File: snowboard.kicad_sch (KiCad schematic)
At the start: 62 parts, among them J1 Micro USB Port, J2 B2B-PH-K-S, Q1 S8050, Q2 S8050, SW1 BOOT, SW2 RESET, U1 ESP32-WROVER-E-N4R8, U2 CP2102N-A02-GQFN28R, U3 SPX3819M5-L-3-3, U4 MCP73831T-2ACI_OT, U5 MPU-6050

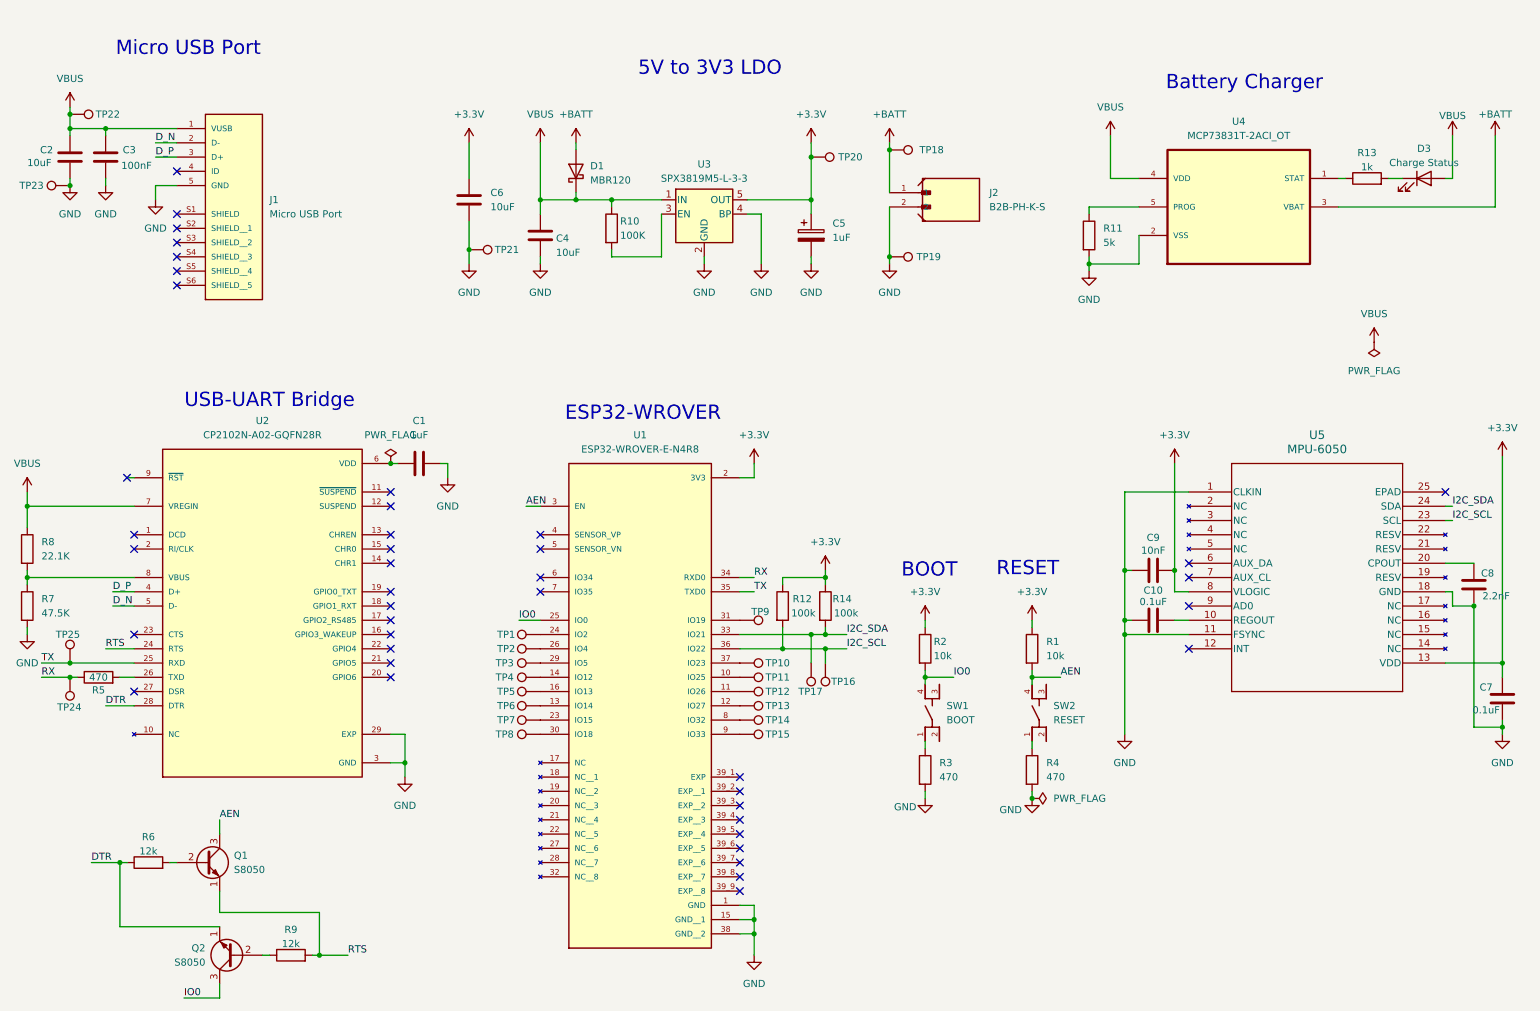
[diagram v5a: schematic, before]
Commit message: Swap discontinued MPU6050 for BNO086
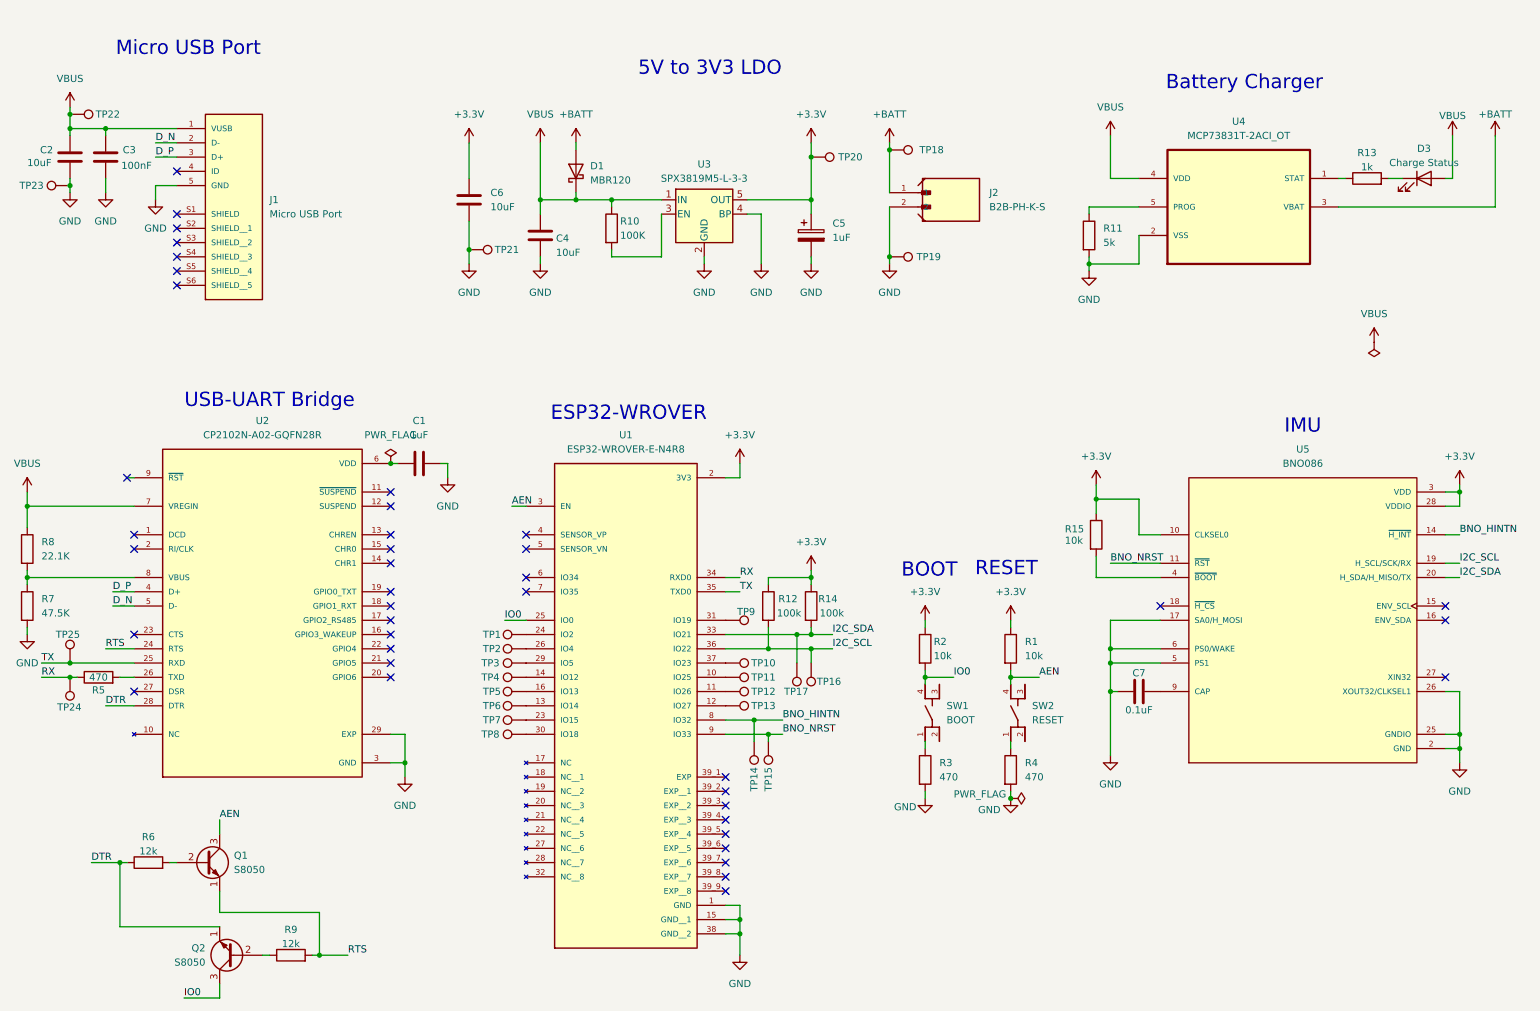
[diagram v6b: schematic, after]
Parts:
- removed C10: 0.1uF, symbol Device:C
- removed C8: 2.2nF, symbol Device:C
- removed C9: 10nF, symbol Device:C
- removed U5: MPU-6050, QFN24_4X4X0P9-0P5_TDK, symbol MPU6050:MPU-6050
- added R15: 10k, symbol Device:R
- added U5: BNO086, BNO080:IC_BNO080, symbol BNO086:BNO080
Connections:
- net +3.3V: now also R15.1, U5.10 (CLKSEL0), U5.28 (VDDIO), U5.3 (VDD); no longer C7.1
- net GND: now also C7.1, U5.17 (SA0/H_MOSI), U5.2 (GND), U5.25 (GNDIO), U5.26 (XOUT32/CLKSEL1), U5.5 (PS1), U5.6 (PS0/WAKE); no longer C7.2
- net I2C_SCL: now also U5.19 (H_SCL/SCK/RX)
- net I2C_SDA: now also U5.20 (H_SDA/H_MISO/TX)
- net BNO_NRST: now reaches TP15.1, U1.9 (IO33)
- net BNO_NRST: now also U5.11 (~{RST})
- net BNO_HINTN: now reaches TP14.1, U1.8 (IO32)
- net BNO_HINTN: now also U5.14 (~{H_INT})
- new net: R15.2, U5.4 (~{BOOT})
- new net: C7.2, U5.9 (CAP)
- no-connect marks 42 -> 41
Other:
- note added: "IMU"
- moved on the sheet: R1, R12, R14, R4, SW2, TP1, TP10, TP11, TP12, TP13, TP14, TP15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

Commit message: Reduce i2c pull-up value, fix shorting LDO, DNP auto-reset
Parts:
- Q1, Q2: now not fitted
- R12, R14: value 100k -> 5k
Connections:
- net GND: no longer U3.4 (BP)
- no-connect marks 41 -> 42
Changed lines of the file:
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@@
 (kicad_sch
-	(version 20231120)
+	(version 20250114)
 	(generator "eeschema")
-	(generator_version "8.0")
+	(generator_version "9.0")
 	(paper "A4")
+	(text "USB-UART Bridge\n"
+		(exclude_from_sim no)
+		(at 62.23 89.154 0)
+		(effects
+			(font
+				(size 2.54 2.54)
+			)
+		)
+	)
+	(text "IMU\n"
+		(exclude_from_sim no)
+		(at 246.38 93.726 0)
+		(effects
+			(font
+				(size 2.54 2.54)
+			)
+		)
+	)
+	(text "Battery Charger\n"
+		(exclude_from_sim no)
+		(at 235.966 32.512 0)
+		(effects
+			(font
+				(size 2.54 2.54)
+			)
+		)
+	)
+	(text "Micro USB Port\n"
+		(exclude_from_sim no)
+		(at 47.752 26.416 0)
+		(effects
+			(font
+				(size 2.54 2.54)
+			)
+		)
+	)
+	(text "ESP32-WROVER\n"
+		(exclude_from_sim no)
+		(at 126.238 91.44 0)
+		(effects
+			(font
+				(size 2.54 2.54)
+			)
+		)
+	)
+	(text "RESET\n"
+		(exclude_from_sim no)
+		(at 193.548 119.126 0)
+		(effects
+			(font
+				(size 2.54 2.54)
+			)
+		)
+	)
+	(text "5V to 3V3 LDO\n\n"
+		(exclude_from_sim no)
+		(at 140.716 32.004 0)
+		(effects
+			(font
+				(size 2.54 2.54)
+			)
+		)
+	)
+	(text "BOOT"
+		(exclude_from_sim no)
+		(at 179.832 119.38 0)
+		(effects
+			(font
+				(size 2.54 2.54)
+			)
+		)
+	)
 	(junction
 		(at 26.67 38.1)
@@
 	)
 	(no_connect
+		(at 147.32 55.88)
+	)
+	(no_connect
 		(at 107.95 120.65)
 	)
@@
 	(wire
 		(pts
-			(xy 149.86 55.88) (xy 149.86 64.77)
-		)
-		(stroke
-			(width 0)
-			(type default)
-		)
-	)
-	(wire
-		(pts
 			(xy 26.67 38.1) (xy 26.67 36.83)
 		)
@@
 	(wire
 		(pts
-			(xy 147.32 55.88) (xy 149.86 55.88)
-		)
-		(stroke
-			(width 0)
-			(type default)
-		)
-	)
-	(wire
-		(pts
 			(xy 110.49 43.18) (xy 110.49 53.34)
 		)
@@
 		)
 	)
-	(text "USB-UART Bridge\n"
-		(exclude_from_sim no)
-		(at 62.23 89.154 0)
-		(effects
-			(font
-				(size 2.54 2.54)
-			)
-		)
-	)
-	(text "IMU\n"
-		(exclude_from_sim no)
-		(at 246.38 93.726 0)
-		(effects
-			(font
-				(size 2.54 2.54)
-			)
-		)
-	)
-	(text "Battery Charger\n"
-		(exclude_from_sim no)
-		(at 235.966 32.512 0)
-		(effects
-			(font
-				(size 2.54 2.54)
-			)
-		)
-	)
-	(text "Micro USB Port\n"
-		(exclude_from_sim no)
-		(at 47.752 26.416 0)
-		(effects
-			(font
-				(size 2.54 2.54)
-			)
-		)
-	)
-	(text "ESP32-WROVER\n"
-		(exclude_from_sim no)
-		(at 126.238 91.44 0)
-		(effects
-			(font
-				(size 2.54 2.54)
-			)
-		)
-	)
-	(text "RESET\n"
-		(exclude_from_sim no)
-		(at 193.548 119.126 0)
-		(effects
-			(font
-				(size 2.54 2.54)
-			)
-		)
-	)
-	(text "5V to 3V3 LDO\n\n"
-		(exclude_from_sim no)
-		(at 140.716 32.004 0)
-		(effects
-			(font
-				(size 2.54 2.54)
-			)
-		)
-	)
-	(text "BOOT"
-		(exclude_from_sim no)
-		(at 179.832 119.38 0)
-		(effects
-			(font
-				(size 2.54 2.54)
-			)
-		)
-	)
 	(label "IO0"
 		(at 46.99 195.58 0)
@@
 			)
 		)
-		(property "Value" "100k"
+		(property "Value" "5k"
 			(at 152.654 127 0)
 			(effects
@@
 		(in_bom yes)
 		(on_board yes)
-		(dnp no)
+		(dnp yes)
 		(fields_autoplaced yes)
 		(property "Reference" "Q2"
@@
 		(in_bom yes)
 		(on_board yes)
-		(dnp no)
+		(dnp yes)
 		(fields_autoplaced yes)
 		(property "Reference" "Q1"
@@
 			)
 		)
-		(property "Value" "100k"
+		(property "Value" "5k"
 			(at 160.274 127 0)
 			(effects
@@
 	)
 	(symbol
-		(lib_id "power:GND")
-		(at 149.86 64.77 0)
-		(unit 1)
-		(exclude_from_sim no)
-		(in_bom yes)
-		(on_board yes)
-		(dnp no)
-		(fields_autoplaced yes)
-		(property "Reference" "#PWR020"
-			(at 149.86 71.12 0)
-			(effects
-				(font
-					(size 1.27 1.27)
-				)
-				(hide yes)
-			)
-		)
-		(property "Value" "GND"
-			(at 149.86 69.85 0)
-			(effects
-				(font
-					(size 1.27 1.27)
-				)
-			)
-		)
-		(property "Footprint" ""
-			(at 149.86 64.77 0)
-			(effects
-				(font
-					(size 1.27 1.27)
-				)
-				(hide yes)
-			)
-		)
-		(property "Datasheet" ""
-			(at 149.86 64.77 0)
-			(effects
-				(font
-					(size 1.27 1.27)
-				)
-				(hide yes)
-			)
-		)
-		(property "Description" "Power symbol creates a global label with name \"GND\" , ground"
-			(at 149.86 64.77 0)
-			(effects
-				(font
-					(size 1.27 1.27)
-				)
-				(hide yes)
-			)
-		)
-		(pin "1"
-		)
-		(instances
-			(project ""
-				(path "/5f320113-62d9-4623-942f-a3d460960b0e"
-					(reference "#PWR020")
-					(unit 1)
-				)
-			)
-		)
-	)
-	(symbol
 		(lib_id "power:+3.3V")
 		(at 158.75 43.18 0)
@@
 		)
 	)
+	(embedded_fonts no)
 )
